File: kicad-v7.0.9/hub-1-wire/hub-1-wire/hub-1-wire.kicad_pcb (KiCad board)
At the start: 2 copper layers, 48.3 x 45.7 mm, 24 parts, among them J1 RJ45, J2 Screw_Terminal_01x03, J3 Screw_Terminal_01x03, J4 Screw_Terminal_01x03, J5 Screw_Terminal_01x03, J6 Screw_Terminal_01x03, J7 Screw_Terminal_01x03, Q1 YJL3415A

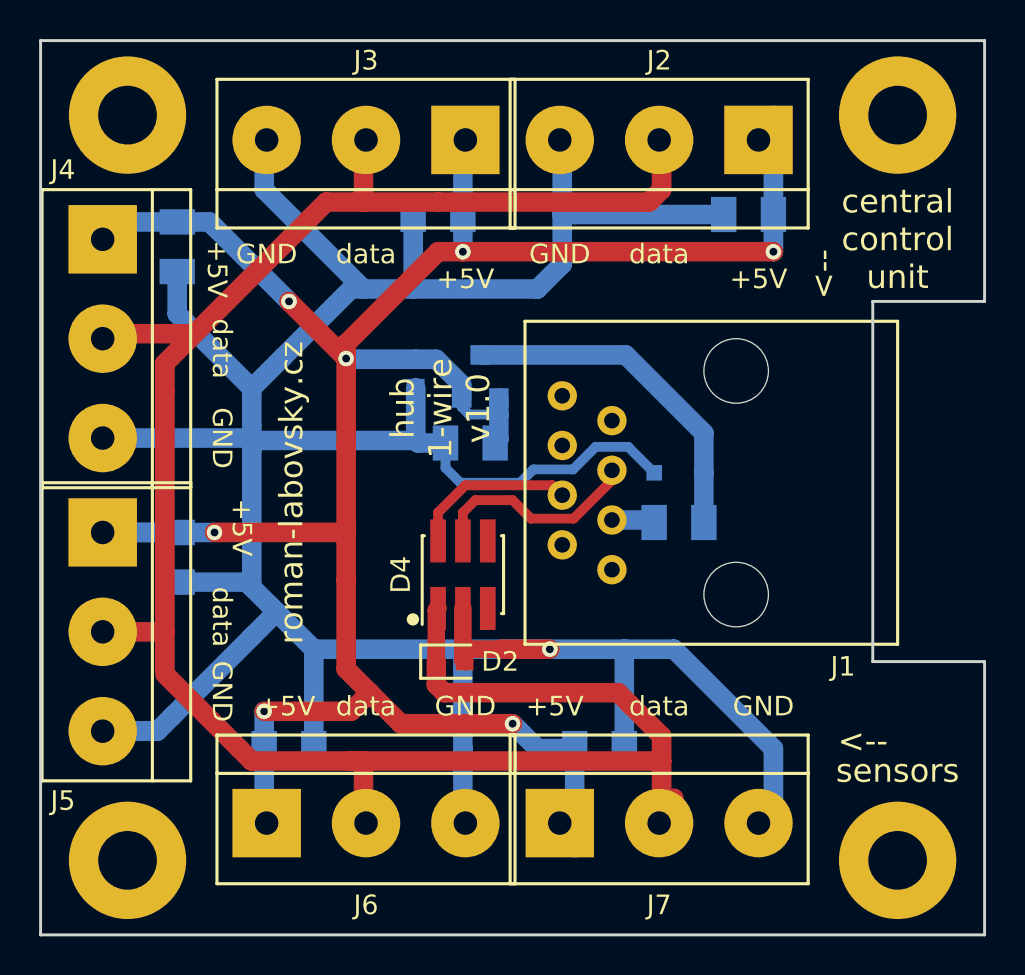
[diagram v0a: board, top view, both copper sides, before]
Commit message: 1-Wire bus hub. Change library. Small changes in schematic a PCB.
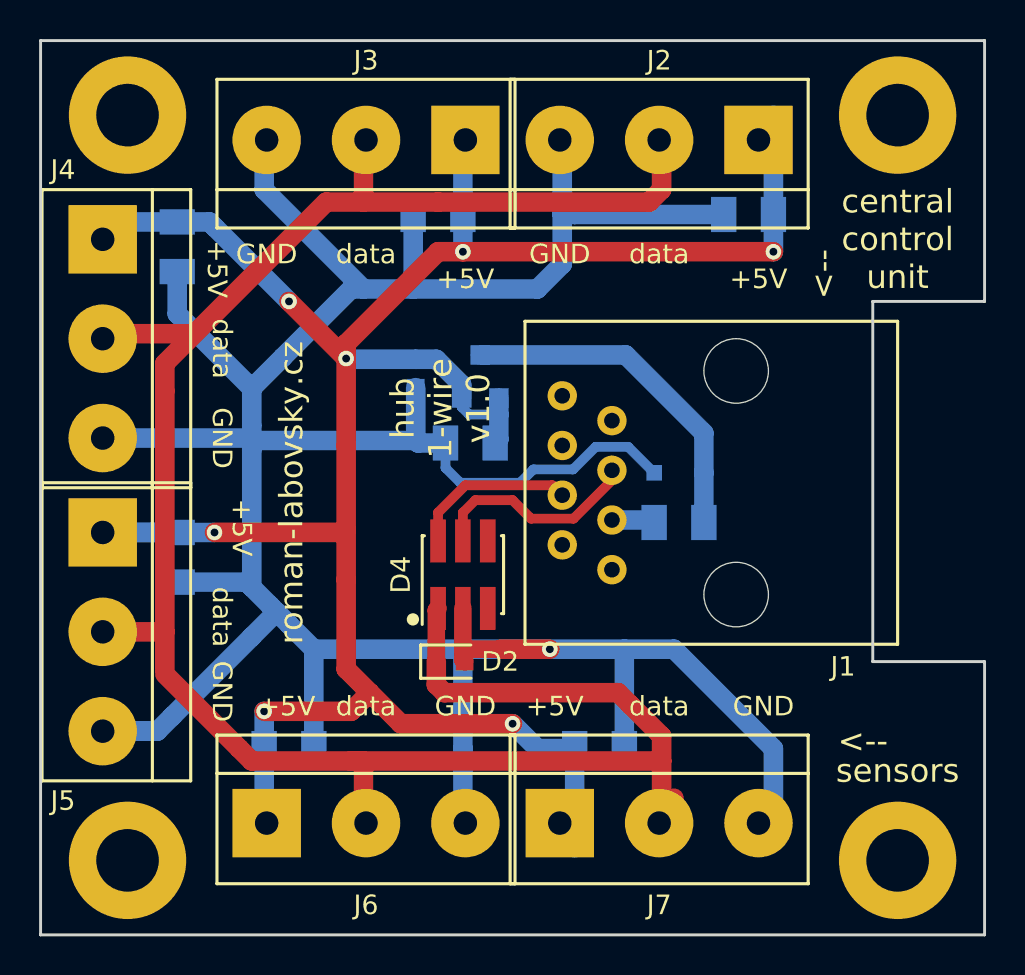
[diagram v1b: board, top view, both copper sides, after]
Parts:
- removed ~ (x4): pad_3x6mm, pad_rl:pad_3x6mm
- added H1: mounting_hole_pad_3.2x6mm, mounting_hole_pad_rl:mounting_hole_pad_3.2x6mm, F.Cu at (135.6, 69.6)
- added H2: mounting_hole_pad_3.2x6mm, mounting_hole_pad_rl:mounting_hole_pad_3.2x6mm, F.Cu at (175.0, 69.6)
- added H3: mounting_hole_pad_3.2x6mm, mounting_hole_pad_rl:mounting_hole_pad_3.2x6mm, F.Cu at (135.6, 107.7)
- added H4: mounting_hole_pad_3.2x6mm, mounting_hole_pad_rl:mounting_hole_pad_3.2x6mm, F.Cu at (175.0, 107.7)
- D4: value DS9503 -> DS9503_us
- J1: value RJ45 -> 54601-908WPLF
- J2, J3, J4, J5, J6, J7: value Screw_Terminal_01x03 -> EBBA-03-C-SS-BU

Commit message: Change of components from edited library.
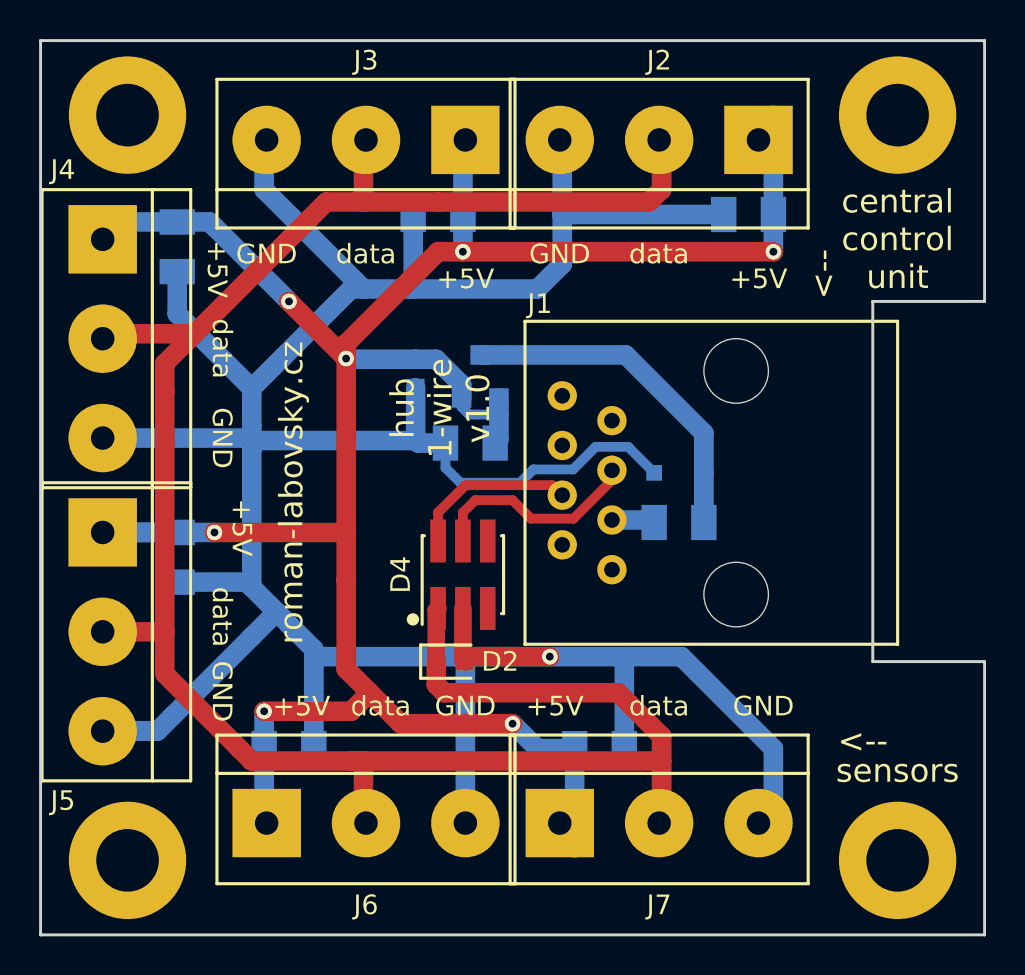
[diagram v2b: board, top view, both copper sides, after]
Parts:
- J1: footprint connector_rl:rj45_54601-908WPLF -> connector_rj45_tht_rl:54601-908WPLF
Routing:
- net GND: track 176.8 -> 174.8 mm
- net Net-(D2-K): track 116.7 -> 114.9 mm
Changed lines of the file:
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@@
   (net 17 "unconnected-(H3-Pad1)")
   (net 18 "unconnected-(H4-Pad1)")
-  (footprint "connector_rl:rj45_54601-908WPLF" (layer "F.Cu")
+  (footprint "connector_rj45_tht_rl:54601-908WPLF" (layer "F.Cu")
     (at 166.751 88.392 90)
-    (descr "RJ45 54601-908WPLF (https://www.amphenol-icc.com/modular-jack-54601908wplf.html)")
+    (descr "RJ45 54601-908WPLF")
     (tags "rj45 908wplf")
     (property "Sheetfile" "hub-1-wire.kicad_sch")
@@
     (property "ki_keywords" "RJ female connector")
     (attr through_hole)
-    (fp_text reference "J1" (at -9.398 5.461) (layer "F.SilkS")
+    (fp_text reference "J1" (at 9.144 -10.033 180) (layer "F.SilkS")
         (effects (font (size 1 1) (thickness 0.16)))
     )
-    (fp_text value "54601-908WPLF" (at 0 9.525 -90) (layer "F.Fab")
-        (effects (font (size 1 1) (thickness 0.15)))
-    )
-    (fp_text user "${REFERENCE}" (at 0 -2.54 -90) (layer "F.Fab")
+    (fp_text value "54601-908WPLF" (at 0 6.35 90) (layer "F.Fab")
+        (effects (font (size 1 1) (thickness 0.15)))
+    )
+    (fp_text user "${REFERENCE}" (at 0 0 90) (layer "F.Fab")
         (effects (font (size 1 1) (thickness 0.15)))
     )
@@
     (fp_line (start 7.62 7.88) (end -7.62 7.88)
       (stroke (width 0.05) (type solid)) (layer "F.Fab"))
-    (pad "" np_thru_hole circle (at -5.716 0 90) (size 3.3 3.3) (drill 3.3) (layers "*.Cu" "*.SilkS" "*.Mask"))
-    (pad "" np_thru_hole circle (at 5.716 0 90) (size 3.3 3.3) (drill 3.3) (layers "*.Cu" "*.SilkS" "*.Mask"))
+    (pad "" np_thru_hole circle (at -5.716 0 90) (size 3.3 3.3) (drill 3.3) (layers "F&B.Cu" "*.Mask"))
+    (pad "" np_thru_hole circle (at 5.716 0 90) (size 3.3 3.3) (drill 3.3) (layers "F&B.Cu" "*.Mask"))
     (pad "1" thru_hole circle (at -4.444 -6.35 90) (size 1.5 1.5) (drill 0.8) (layers "*.Cu" "*.Mask")
       (net 10 "unconnected-(J1-Pad1)") (pintype "passive+no_connect"))
@@
   (footprint "mounting_hole_pad_rl:mounting_hole_pad_3.2x6mm" (layer "F.Cu")
     (at 175.006 107.696)
-    (descr "Mounting hole with pad 3.2 drill, 6 diameter")
+    (descr "Mounting hole with pad 3.2 mm drill, 6 mm diameter")
     (tags "mountig hole pad 3.2x6")
     (property "Sheetfile" "hub-1-wire.kicad_sch")
@@
   (footprint "mounting_hole_pad_rl:mounting_hole_pad_3.2x6mm" (layer "F.Cu")
     (at 175.006 69.596)
-    (descr "Mounting hole with pad 3.2 drill, 6 diameter")
+    (descr "Mounting hole with pad 3.2 mm drill, 6 mm diameter")
     (tags "mountig hole pad 3.2x6")
     (property "Sheetfile" "hub-1-wire.kicad_sch")
@@
   (footprint "mounting_hole_pad_rl:mounting_hole_pad_3.2x6mm" (layer "F.Cu")
     (at 135.636 107.696)
-    (descr "Mounting hole with pad 3.2 drill, 6 diameter")
+    (descr "Mounting hole with pad 3.2 mm drill, 6 mm diameter")
     (tags "mountig hole pad 3.2x6")
     (property "Sheetfile" "hub-1-wire.kicad_sch")
@@
   (footprint "mounting_hole_pad_rl:mounting_hole_pad_3.2x6mm" (layer "F.Cu")
     (at 135.636 69.596)
-    (descr "Mounting hole with pad 3.2 drill, 6 diameter")
+    (descr "Mounting hole with pad 3.2 mm drill, 6 mm diameter")
     (tags "mountig hole pad 3.2x6")
     (property "Sheetfile" "hub-1-wire.kicad_sch")
@@
     (effects (font (size 1 1) (thickness 0.25)))
   )
-  (gr_text "data" (at 147.828 99.822) (layer "F.SilkS")
-    (effects (font (size 1 1) (thickness 0.25)))
-  )
-  (gr_text "+5V" (at 143.764 99.822) (layer "F.SilkS")
+  (gr_text "data" (at 148.59 99.822) (layer "F.SilkS")
+    (effects (font (size 1 1) (thickness 0.25)))
+  )
+  (gr_text "+5V" (at 144.526 99.822) (layer "F.SilkS")
     (effects (font (size 1 1) (thickness 0.25)))
   )
@@
   )
   (segment (start 152.781 94.8182) (end 152.781 96.901) (width 0.9) (layer "F.Cu") (net 1))
-  (segment (start 154.686 96.901) (end 157.226 96.901) (width 1) (layer "F.Cu") (net 1))
+  (segment (start 157.226 97.282) (end 153.416 97.282) (width 1) (layer "F.Cu") (net 1))
   (segment (start 152.781 97.446) (end 152.871 97.536) (width 0.9) (layer "F.Cu") (net 1))
-  (segment (start 154.686 96.901) (end 152.781 96.901) (width 0.9) (layer "F.Cu") (net 1))
   (segment (start 152.781 96.901) (end 152.781 97.446) (width 0.9) (layer "F.Cu") (net 1))
-  (via (at 157.226 96.901) (size 0.8) (drill 0.4) (layers "F.Cu" "B.Cu") (net 1))
+  (via (at 157.226 97.282) (size 0.8) (drill 0.4) (layers "F.Cu" "B.Cu") (net 1))
   (segment (start 141.986 83.566) (end 141.986 85.471) (width 1) (layer "B.Cu") (net 1))
   (segment (start 142.621 73.406) (end 147.701 78.486) (width 1) (layer "B.Cu") (net 1))
@@
   (segment (start 143.891 95.631) (end 143.256 94.996) (width 1) (layer "B.Cu") (net 1))
   (segment (start 137.16 101.092) (end 137.922 100.33) (width 1) (layer "B.Cu") (net 1))
+  (segment (start 152.908 105.791) (end 152.908 97.79) (width 1) (layer "B.Cu") (net 1))
   (segment (start 134.366 86.106) (end 141.986 86.106) (width 1) (layer "B.Cu") (net 1))
   (segment (start 141.732 93.472) (end 141.986 93.726) (width 1) (layer "B.Cu") (net 1))
@@
   (segment (start 155.702 88.392) (end 156.38399 87.71001) (width 0.5) (layer "B.Cu") (net 1))
   (segment (start 147.701 78.486) (end 147.066 78.486) (width 1) (layer "B.Cu") (net 1))
-  (segment (start 161.036 101.981) (end 161.036 96.901) (width 1) (layer "B.Cu") (net 1))
-  (segment (start 168.656 101.981) (end 163.576 96.901) (width 1) (layer "B.Cu") (net 1))
+  (segment (start 161.29 97.282) (end 163.957 97.282) (width 1) (layer "B.Cu") (net 1))
   (segment (start 150.368 83.529) (end 150.368 86.233) (width 1) (layer "B.Cu") (net 1))
   (segment (start 158.412992 87.71001) (end 156.38399 87.71001) (width 0.5) (layer "B.Cu") (net 1))
-  (segment (start 145.161 96.901) (end 161.036 96.901) (width 1) (layer "B.Cu") (net 1))
   (segment (start 145.161 101.981) (end 145.161 96.901) (width 1) (layer "B.Cu") (net 1))
+  (segment (start 145.161 97.282) (end 152.4 97.282) (width 1) (layer "B.Cu") (net 1))
   (segment (start 161.231999 86.555999) (end 159.567003 86.555999) (width 0.5) (layer "B.Cu") (net 1))
   (segment (start 159.567003 86.555999) (end 158.412992 87.71001) (width 0.5) (layer "B.Cu") (net 1))
-  (segment (start 152.781 101.981) (end 152.781 105.791) (width 1) (layer "B.Cu") (net 1))
   (segment (start 150.368 86.233) (end 142.113 86.233) (width 1) (layer "B.Cu") (net 1))
   (segment (start 166.116 74.676) (end 158.496 74.676) (width 1) (layer "B.Cu") (net 1))
+  (segment (start 161.036 101.981) (end 161.036 97.536) (width 1) (layer "B.Cu") (net 1))
   (segment (start 152.654 88.392) (end 155.702 88.392) (width 0.5) (layer "B.Cu") (net 1))
   (segment (start 142.9385 94.6785) (end 141.986 93.726) (width 1) (layer "B.Cu") (net 1))
   (segment (start 162.56 87.884) (end 161.231999 86.555999) (width 0.5) (layer "B.Cu") (net 1))
   (segment (start 138.176 93.472) (end 141.732 93.472) (width 1) (layer "B.Cu") (net 1))
-  (segment (start 152.781 101.981) (end 152.781 96.901) (width 1) (layer "B.Cu") (net 1))
+  (segment (start 163.957 97.282) (end 164.7825 98.1075) (width 1) (layer "B.Cu") (net 1))
   (segment (start 143.891 95.631) (end 145.161 96.901) (width 1) (layer "B.Cu") (net 1))
   (segment (start 143.256 94.996) (end 142.9385 94.6785) (width 1) (layer "B.Cu") (net 1))
@@
   (segment (start 142.113 86.233) (end 141.986 86.106) (width 1) (layer "B.Cu") (net 1))
   (segment (start 151.892 86.36) (end 151.892 87.63) (width 0.5) (layer "B.Cu") (net 1))
+  (segment (start 161.036 97.536) (end 161.29 97.282) (width 1) (layer "B.Cu") (net 1))
   (segment (start 134.366 101.092) (end 136.906 101.092) (width 1) (layer "B.Cu") (net 1))
   (segment (start 157.861 74.676) (end 157.861 77.216) (width 1) (layer "B.Cu") (net 1))
@@
   (segment (start 134.366 101.092) (end 137.16 101.092) (width 1) (layer "B.Cu") (net 1))
   (segment (start 147.066 78.486) (end 143.5735 81.9785) (width 1) (layer "B.Cu") (net 1))
+  (segment (start 168.656 101.981) (end 164.7825 98.1075) (width 1) (layer "B.Cu") (net 1))
   (segment (start 138.176 77.597) (end 138.176 79.756) (width 1) (layer "B.Cu") (net 1))
   (segment (start 141.986 96.266) (end 143.256 94.996) (width 1) (layer "B.Cu") (net 1))
@@
   (segment (start 156.591 78.486) (end 150.241 78.486) (width 1) (layer "B.Cu") (net 1))
   (segment (start 150.241 78.486) (end 147.701 78.486) (width 1) (layer "B.Cu") (net 1))
-  (segment (start 161.036 96.901) (end 163.576 96.901) (width 1) (layer "B.Cu") (net 1))
+  (segment (start 152.4 97.282) (end 161.29 97.282) (width 1) (layer "B.Cu") (net 1))
   (segment (start 157.861 70.866) (end 157.861 74.676) (width 1) (layer "B.Cu") (net 1))
   (segment (start 141.986 86.106) (end 141.986 85.471) (width 1) (layer "B.Cu") (net 1))
@@
   (segment (start 162.941 105.791) (end 162.941 102.616) (width 1) (layer "F.Cu") (net 3))
   (segment (start 162.941 70.866) (end 162.941 73.406) (width 1) (layer "F.Cu") (net 3))
-  (segment (start 163.576 104.521) (end 162.306 105.791) (width 1) (layer "F.Cu") (net 3))
   (segment (start 147.701 70.866) (end 147.701 74.041) (width 1) (layer "F.Cu") (net 3))
   (segment (start 137.541 83.693) (end 137.541 82.296) (width 1) (layer "F.Cu") (net 3))
